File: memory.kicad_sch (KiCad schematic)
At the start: 34 parts, among them U1002 AM6231ASGGGAALW, U4001 K4AAG165WA-BCWE

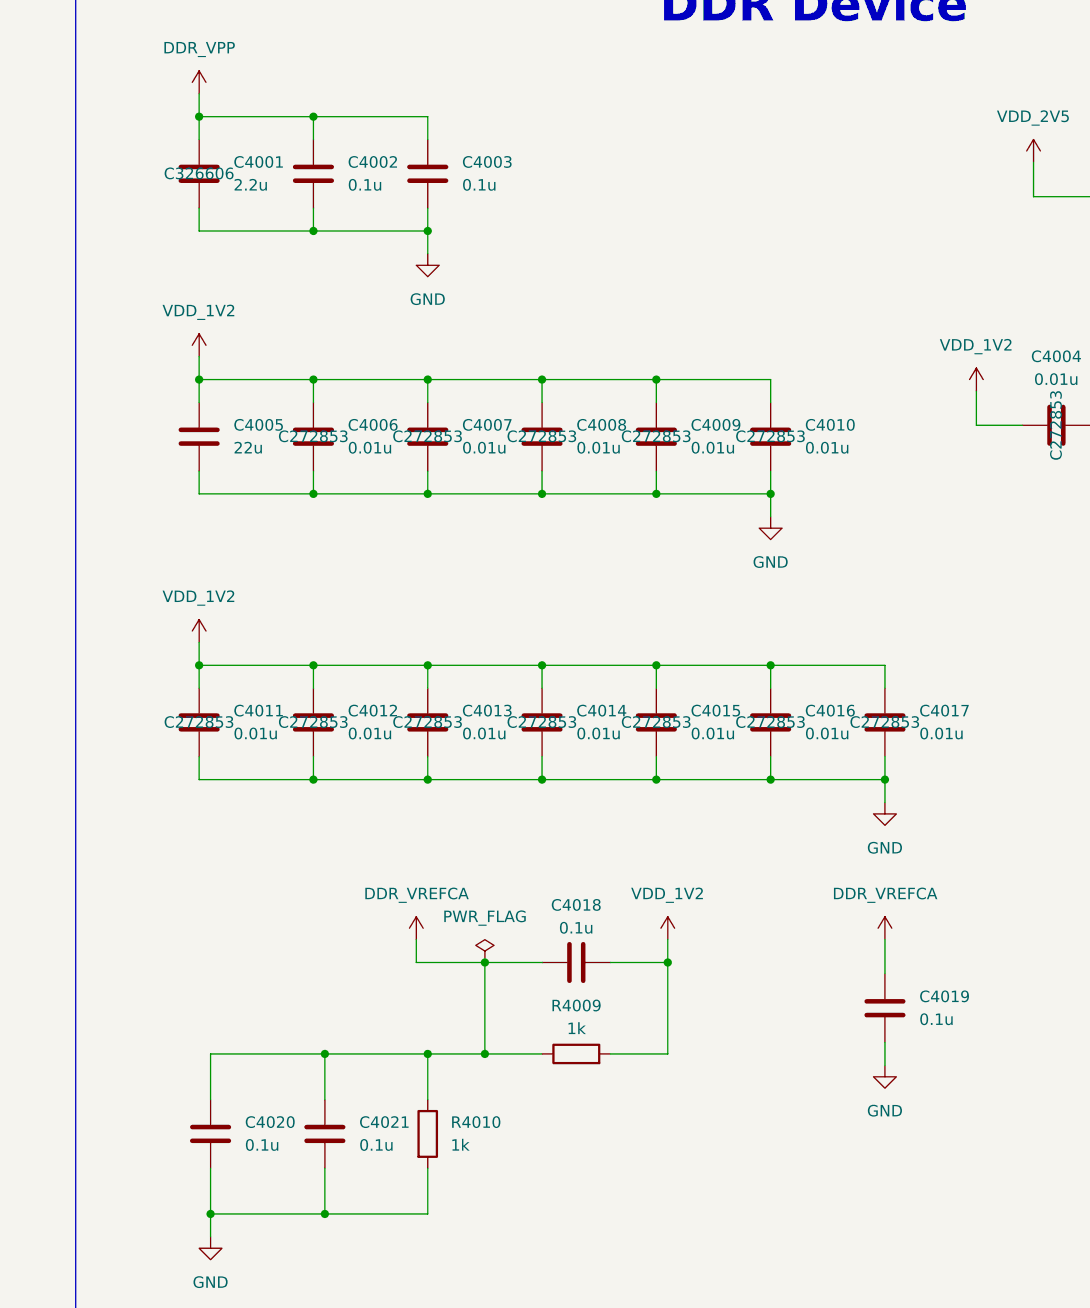
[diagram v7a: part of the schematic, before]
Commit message: All capacitors and crystals added to BOM. 150u cap for USB A changed to tantalum and rerouted
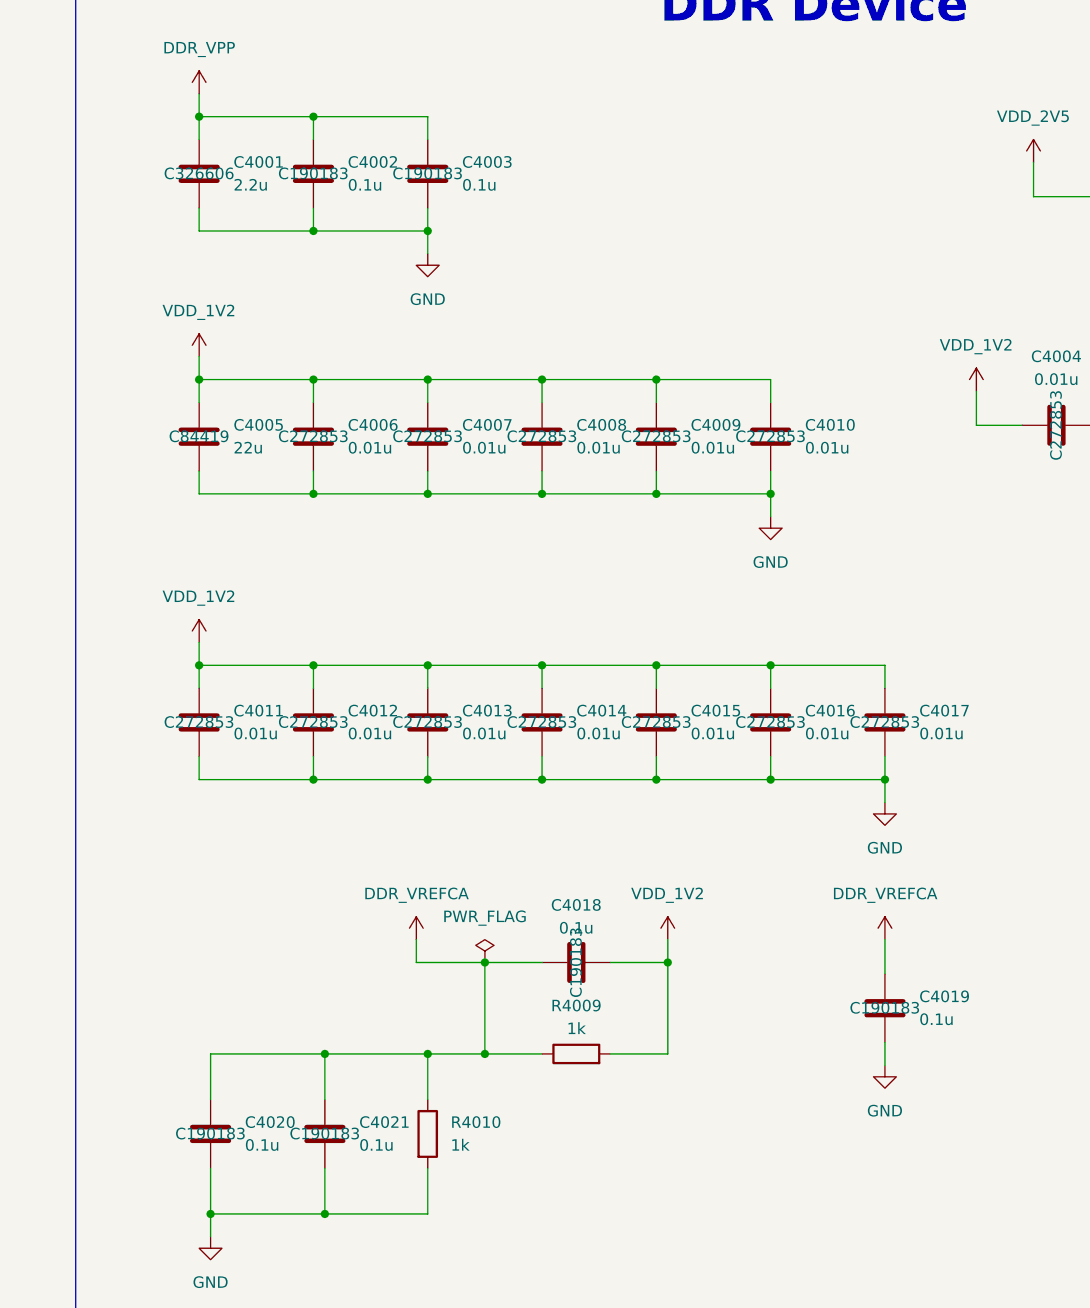
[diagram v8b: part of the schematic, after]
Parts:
- C4002, C4003, C4018, C4019, C4020, C4021: JLCPCB Part# (none) -> C190183
- C4005: JLCPCB Part# (none) -> C84419
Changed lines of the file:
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@@
 			)
 		)
-		(property "JLCPCB Part#" ""
+		(property "JLCPCB Part#" "C190183"
 			(at 455.93 125.73 0)
 			(effects
@@
 			)
 		)
-		(property "JLCPCB Part#" ""
+		(property "JLCPCB Part#" "C84419"
 			(at 430.53 154.94 0)
 			(effects
@@
 			)
 		)
-		(property "JLCPCB Part#" ""
+		(property "JLCPCB Part#" "C190183"
 			(at 506.73 218.44 0)
 			(effects
@@
 			)
 		)
-		(property "JLCPCB Part#" ""
+		(property "JLCPCB Part#" "C190183"
 			(at 472.44 213.36 0)
 			(effects
@@
 			)
 		)
-		(property "JLCPCB Part#" ""
+		(property "JLCPCB Part#" "C190183"
 			(at 431.8 232.41 0)
 			(effects
@@
 			)
 		)
-		(property "JLCPCB Part#" ""
+		(property "JLCPCB Part#" "C190183"
 			(at 444.5 232.41 0)
 			(effects
@@
 			)
 		)
-		(property "JLCPCB Part#" ""
+		(property "JLCPCB Part#" "C190183"
 			(at 443.23 125.73 0)
 			(effects
